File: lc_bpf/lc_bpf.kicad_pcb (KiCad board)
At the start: 2 copper layers, 47 x 47 mm, 27 parts, among them J2 Conn_01x03, J3 Conn_01x03

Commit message: Change filter layout
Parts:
- removed C13, C14: C, Capacitor_SMD:C_0805_2012Metric_Pad1.15x1.40mm_HandSolder
- removed the C2 at (62.9, 76.8)
- removed the C3 at (59.1, 71.1)
- removed the J2 at (66.0, 86.4)
- removed J3: Conn_01x03, Connector_PinHeader_2.54mm:PinHeader_1x03_P2.54mm_Vertical
- removed R1, R2, R3, R4: R, Resistor_SMD:R_0805_2012Metric_Pad1.15x1.40mm_HandSolder
- added H1: ~, MountingHole:MountingHole_3.2mm_M3_Pad, F.Cu at (40.6, 55.9)
- added H2: ~, MountingHole:MountingHole_3.2mm_M3_Pad, F.Cu at (40.6, 76.2)
- added H3: ~, MountingHole:MountingHole_3.2mm_M3_Pad, F.Cu at (106.7, 55.9)
- added H4: ~, MountingHole:MountingHole_3.2mm_M3_Pad, F.Cu at (106.7, 76.2)
- C1: footprint Capacitor_SMD:C_0805_2012Metric_Pad1.15x1.40mm_HandSolder -> Capacitor_SMD:C_1206_3216Metric_Pad1.42x1.75mm_HandSolder
- L1, L5: footprint Inductor_SMD:L_1210_3225Metric_Pad1.42x2.65mm_HandSolder -> lc_bpf:L
- moved J1 27.0 mm to (40.6, 66.0)
- moved J2 27.0 mm to (106.7, 66.0)
- moved L5 15.0 mm to (96.5, 63.5), turned to 90 degrees
- moved C1 14.8 mm to (58.4, 71.1), turned to 0 degrees
- moved L1 14.6 mm to (50.8, 63.5), turned to 90 degrees
- moved C10 0.64 mm to (88.9, 71.1)
- moved C3 0.64 mm to (66.0, 71.1)
- moved C8 0.64 mm to (81.3, 71.1)
- renumbered C12 to C10, C4 to C2, C5 to C3, C6 to C4, C7 to C5, C8 to C6, C9 to C7, C10 to C8, C11 to C9, J4 to J2
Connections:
- C2 pad 1: Net-(C3-Pad1) -> Net-(C1-Pad1)
- J1 pad 1: Net-(C3-Pad1) -> Net-(C1-Pad1)
- L1 pad 1: Net-(C3-Pad1) -> Net-(C1-Pad1)
- L1 pad 2: Net-(C2-Pad1) -> GND
- L2 pad 1: Net-(C3-Pad1) -> Net-(C1-Pad1)
- L5 pad 2: Net-(C13-Pad1) -> GND
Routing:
- net Net-(C1-Pad1): track 0.00 -> 29.0 mm
- net Net-(C10-Pad1): track 10.0 -> 29.0 mm
- net Net-(C3-Pad1): track 10.0 -> 0.00 mm
- net Net-(C6-Pad2): track 19.3 -> 18.3 mm
- net GND: vias 80 -> 329
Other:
- board size 47 x 47 mm -> 81.3 x 35.6 mm
- board text added: "General purpose filter board"
- board text added: "OH2EAT 2019"

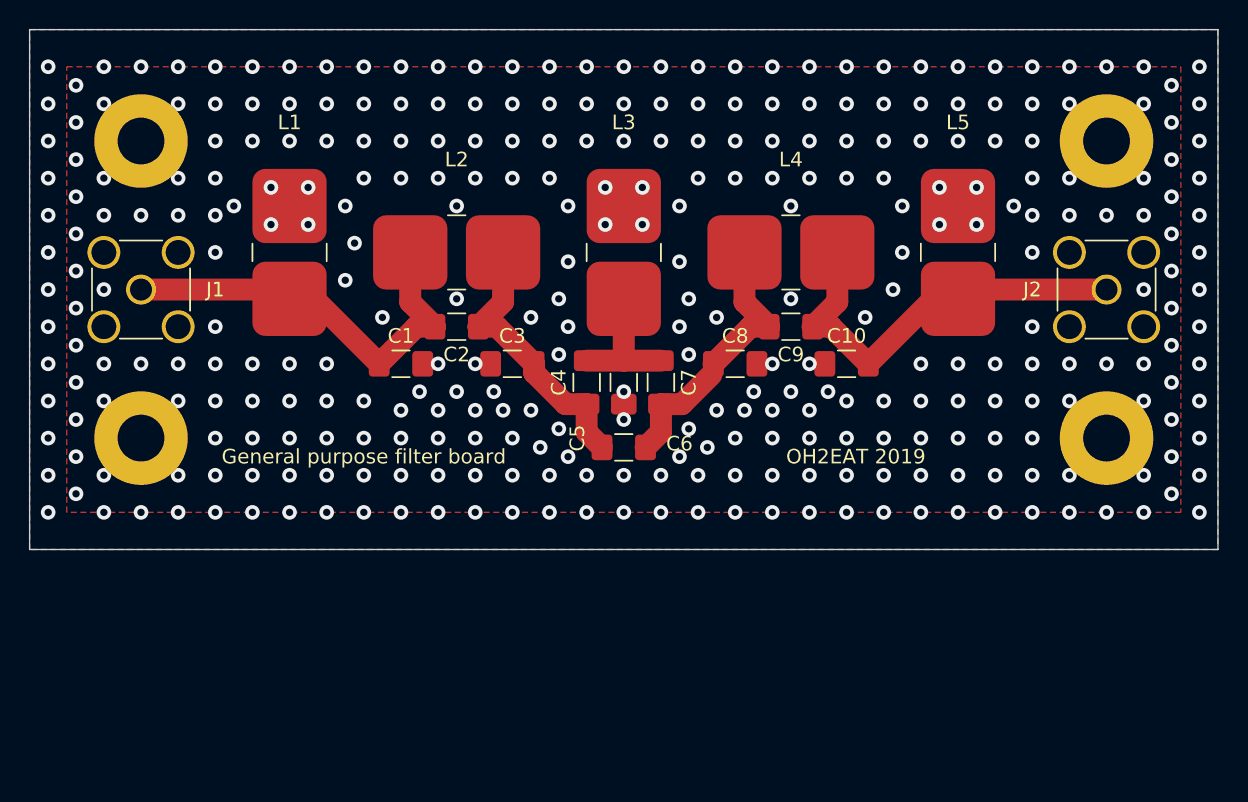
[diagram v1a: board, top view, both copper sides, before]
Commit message: Filter board done
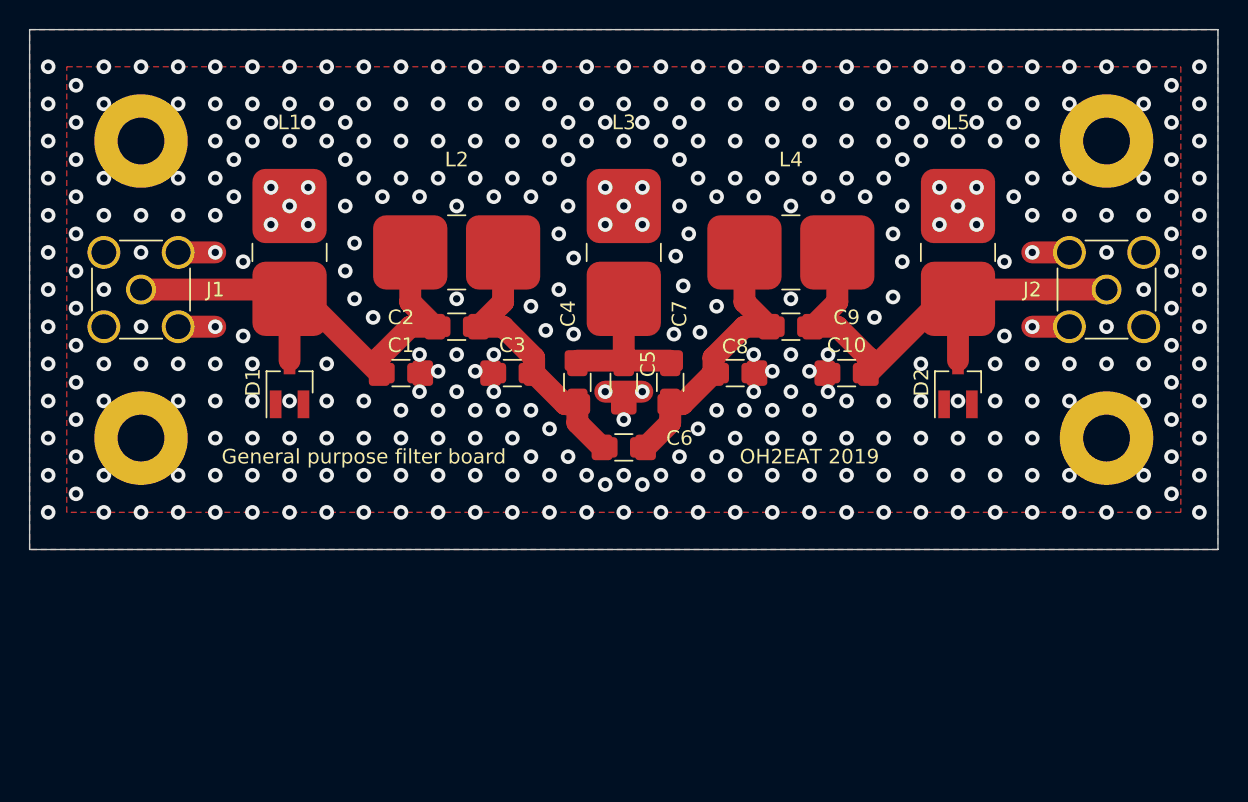
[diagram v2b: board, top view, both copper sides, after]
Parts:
- added D1: D_x2_Serial_AKC, Package_TO_SOT_SMD:SOT-23_Handsoldering, F.Cu at (50.8, 72.4)
- added D2: D_x2_Serial_AKC, Package_TO_SOT_SMD:SOT-23_Handsoldering, F.Cu at (96.5, 72.4)
- C1, C10, C2, C3, C4, C5, C6, C7, C8, C9: footprint Capacitor_SMD:C_1206_3216Metric_Pad1.42x1.75mm_HandSolder -> lc_bpf:C
- moved C4 0.64 mm to (70.5, 72.4)
- moved C1 0.63 mm to (58.4, 71.8)
- moved C10 0.63 mm to (88.9, 71.8)
- moved C3 0.63 mm to (66.0, 71.8)
- moved C7 0.63 mm to (76.8, 72.4)
- moved C8 0.63 mm to (81.3, 71.8)
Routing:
- net GND: track 0.00 -> 12.7 mm, vias 329 -> 376
- net Net-(C10-Pad1): track 29.0 -> 36.1 mm
- net Net-(C1-Pad1): track 29.0 -> 34.4 mm
- net Net-(C4-Pad2): track 9.31 -> 10.6 mm
- net Net-(C6-Pad2): track 18.3 -> 19.0 mm
